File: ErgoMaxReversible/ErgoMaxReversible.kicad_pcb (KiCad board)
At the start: 2 copper layers, 182.8 x 169.2 mm, 102 parts, among them J1 PJ-320A, K1 KEYSW, K10 KEYSW, K11 KEYSW, K12 KEYSW, K13 KEYSW, K14 KEYSW, K15 KEYSW, K16 KEYSW, K17 KEYSW, K18 KEYSW, K19 KEYSW, K2 KEYSW, K20 KEYSW, K21 KEYSW, K22 KEYSW, K23 KEYSW, K24 KEYSW, K25 KEYSW, K26 KEYSW, K27 KEYSW, K28 KEYSW, K29 KEYSW, K3 KEYSW, K30 KEYSW, K31 KEYSW, K32 KEYSW, K33 KEYSW, K34 KEYSW, K35 KEYSW, K36 KEYSW, K37 KEYSW, K38 KEYSW, K39 KEYSW, K4 KEYSW, K40 KEYSW, K41 KEYSW, K42 KEYSW, K43 KEYSW, K44 KEYSW, K5 KEYSW, K6 KEYSW, K7 KEYSW, K8 KEYSW, K9 KEYSW, U1 ProMicro

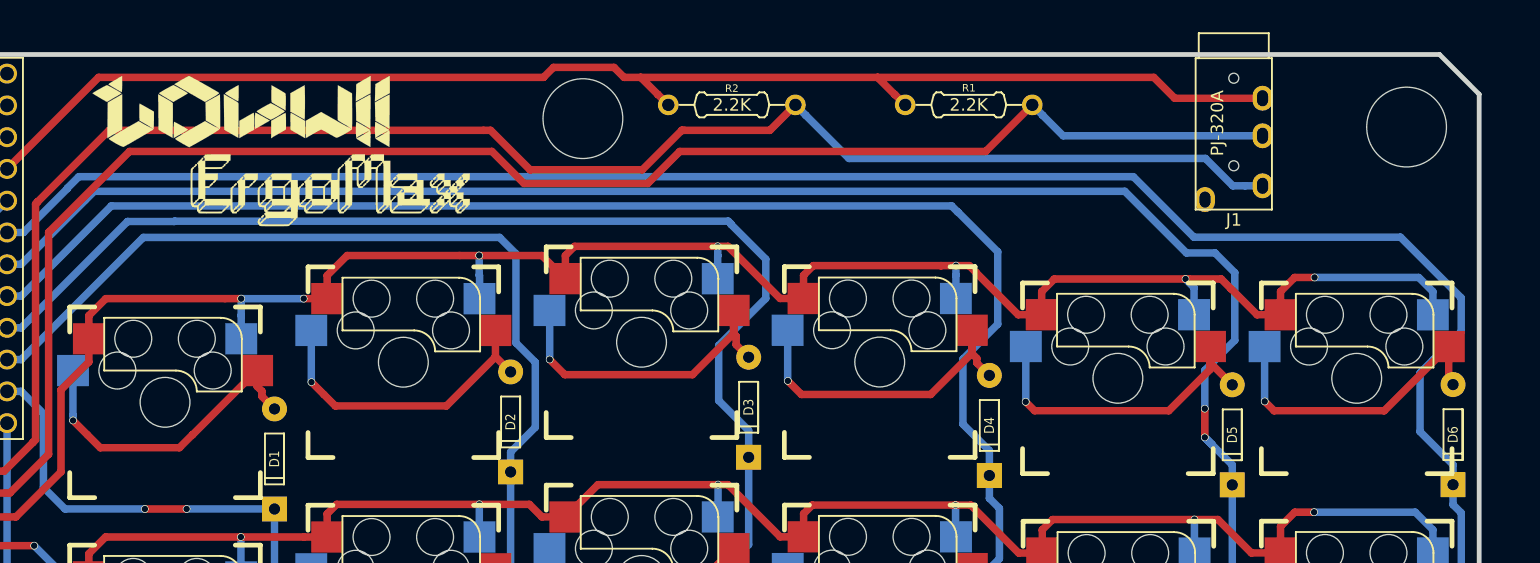
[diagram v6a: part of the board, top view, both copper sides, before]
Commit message: update jack connector to be reversible; add logos on back of the pcb - reversible pcb
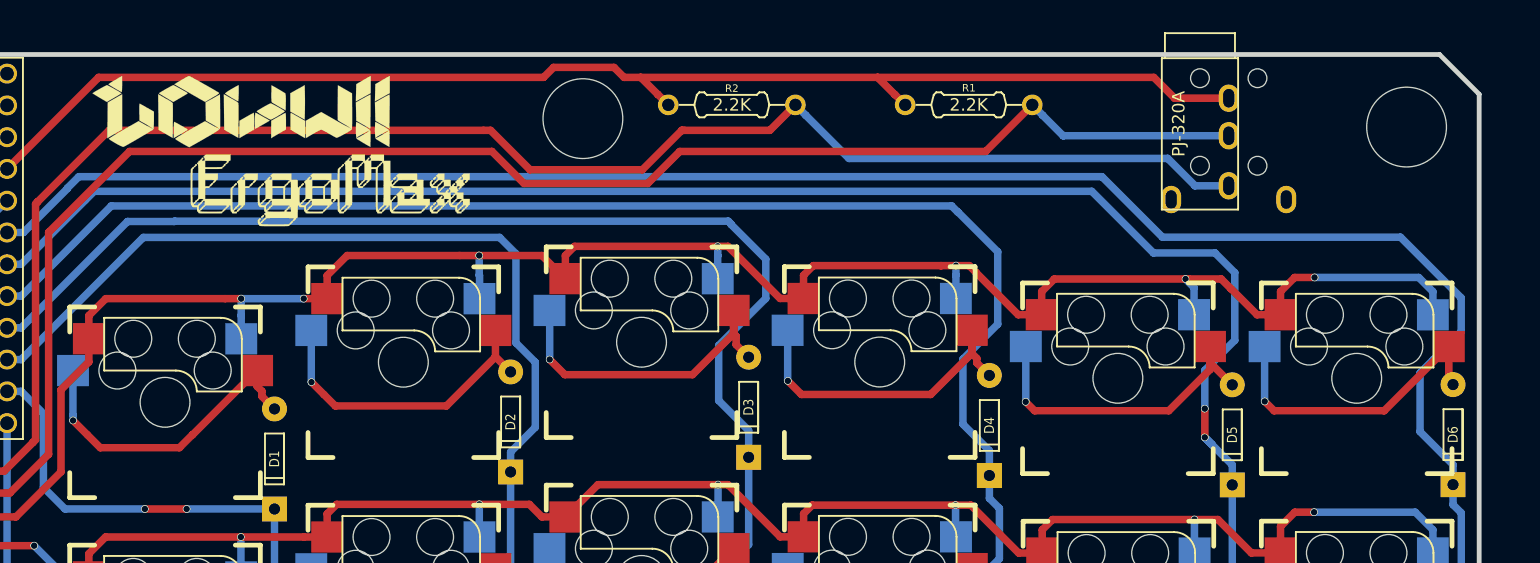
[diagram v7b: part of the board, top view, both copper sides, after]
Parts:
- added Lg3: Logo, ErgoMax:LouWii-logo, B.Cu at (155.4, 40.7)
- added Lg4: Logo, ErgoMax:ErgoMax-logo, B.Cu at (161.8, 46.8)
- J1: footprint Keebio-Parts:TRRS-PJ-320A-no-Fmask -> Keebio-Parts:TRRS-PJ-320A-dual
- moved J1 0.40 mm to (233.6, 36.1)
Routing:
- net VCC: track 111.0 -> 108.3 mm
- net SCL: track 160.7 -> 158.0 mm
- net SDA: track 163.4 -> 160.7 mm

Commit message: add footprints for reversible diode with and without 3d model and use it on reversible pcb
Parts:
- D1, D10, D11, D12, D13, D14, D15, D16, D17, D18, D19, D2, D20, D21, D22, D23, D24, D25, D26, D27, D28, D29, D3, D30, D31, D32, D33, D34, D35, D36, D37, D38, D39, D4, D40, D41, D42, D43, D44, D5, D6, D7, D8, D9: footprint Keebio-Parts:Diode_Long -> ErgoMax:Diode_Long_Reversible-No3dModel
